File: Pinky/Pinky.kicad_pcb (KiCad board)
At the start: 2 copper layers, 142.2 x 120.5 mm, 79 parts, among them J1 MJ-4PP-9, J4 LED, P1 i2c-pin, P2 i2c-pin, SW1 RESET_SW, SW10 SW_PUSH, SW11 SW_PUSH, SW12 SW_PUSH, SW13 SW_PUSH, SW14 SW_PUSH, SW15 SW_PUSH, SW16 SW_PUSH, SW17 SW_PUSH, SW18 SW_PUSH, SW19 SW_PUSH, SW2 SW_PUSH, SW20 SW_PUSH, SW21 SW_PUSH, SW22 SW_PUSH, SW23 SW_PUSH, SW24 SW_PUSH, SW25 SW_PUSH, SW26 SW_PUSH, SW27 SW_PUSH, SW28 SW_PUSH, SW29 SW_PUSH, SW3 SW_PUSH, SW30 SW_PUSH, SW31 SW_PUSH, SW32 SW_PUSH, SW33 SW_PUSH, SW4 SW_PUSH, SW5 SW_PUSH, SW6 SW_PUSH, SW7 SW_PUSH, SW8 SW_PUSH, SW9 SW_PUSH, U1 ProMicro

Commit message: finished wiring
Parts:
- removed J4: LED, kbd:StripLED_rev
- JP1: value Jumper -> JP
- moved JP1 4.81 mm to (82.2, 133.8)
- moved D31 1.90 mm to (164.3, 104.2)
- moved D22 0.28 mm to (129.6, 119.7)
- moved D15 0.20 mm to (107.2, 90.2)
- moved D21 0.10 mm to (126.2, 96.5)
- turned R1 to 180 degrees
- turned R2 to 180 degrees
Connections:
- U1 pad 1: led -> Net-(U1-Pad1)
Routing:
- net GND: track 6.44 -> 179.2 mm, vias 0 -> 34
- net VCC: track 29.3 -> 151.1 mm, vias 0 -> 1
- net col6: track 184.9 -> 298.2 mm, vias 6 -> 8
- net Net-(J1-PadB): track 6.44 -> 115.2 mm, vias 0 -> 1
- net col5: track 185.0 -> 289.9 mm, vias 6 -> 7
- net row3: track 94.7 -> 182.5 mm, vias 0 -> 1
- net row0: track 159.4 -> 231.3 mm, vias 0 -> 1
- net row4: track 63.7 -> 125.2 mm, vias 0 -> 2
- net data: track 0.00 -> 53.4 mm, vias 0 -> 1
- net reset: track 0.00 -> 50.5 mm, vias 0 -> 1
- net sda: track 0.00 -> 47.1 mm, vias 0 -> 1
- net scl: track 0.00 -> 44.5 mm, vias 0 -> 1
- net Net-(D4-Pad2): track 61.8 -> 18.6 mm, vias 4 -> 1
- net col3: track 221.7 -> 255.6 mm, vias 6 -> 7
- net col4: track 236.8 -> 270.4 mm, vias 9 -> 7
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- added copper zone on B.Cu, net GND
- added copper zone on F.Cu, net GND
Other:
- net class Default: via_dia 0.8 -> 0.6
- board text added: "ver. 0.1.0. @tamanishi"

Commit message: add top plate layer
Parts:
- moved D26 0.05 mm to (145.2, 100.2)
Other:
- board text added: "rev. 0.1 @tamanishi"
- board text removed: "ver. 0.1.0. @tamanishi"
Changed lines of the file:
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@@
   (general
     (thickness 1.6)
-    (drawings 151)
+    (drawings 172)
     (tracks 1427)
     (zones 0)
@@
   (page A4)
   (layers
-    (0 F.Cu signal hide)
-    (31 B.Cu signal hide)
+    (0 F.Cu signal)
+    (31 B.Cu signal)
     (32 B.Adhes user hide)
     (33 F.Adhes user hide)
-    (34 B.Paste user hide)
+    (34 B.Paste user)
     (35 F.Paste user hide)
-    (36 B.SilkS user hide)
-    (37 F.SilkS user hide)
+    (36 B.SilkS user)
+    (37 F.SilkS user)
     (38 B.Mask user hide)
     (39 F.Mask user hide)
@@
     (41 Cmts.User user hide)
     (42 Eco1.User user hide)
-    (43 Eco2.User user)
+    (43 Eco2.User user hide)
     (44 Edge.Cuts user)
     (45 Margin user hide)
@@
     (pad_to_mask_clearance 0.051)
     (solder_mask_min_width 0.25)
-    (aux_axis_origin 0 0)
+    (aux_axis_origin 40.3 35.2)
     (visible_elements FFFFFF3F)
     (pcbplotparams
@@
   )
   (module kbd:D3_TH_SMD (layer F.Cu)
-    (at 145.2 100.2)
+    (at 145.25 100.2)
     (descr "Resitance 3 pas")
     (tags R)
@@
       (net 50 col6))
   )
-  (gr_text "ver. 0.1.0.\n@tamanishi" (at 83.2 121.2) (layer B.SilkS)
+  (dimension 142.2 (width 0.3) (layer Dwgs.User)
+    (gr_text "142.200 mm" (at 111.4 29.8) (layer Dwgs.User)
+      (effects (font (size 1.5 1.5) (thickness 0.3)))
+    )
+    (feature1 (pts (xy 182.5 35.2) (xy 182.5 31.313579)))
+    (feature2 (pts (xy 40.3 35.2) (xy 40.3 31.313579)))
+    (crossbar (pts (xy 40.3 31.9) (xy 182.5 31.9)))
+    (arrow1a (pts (xy 182.5 31.9) (xy 181.373496 32.486421)))
+    (arrow1b (pts (xy 182.5 31.9) (xy 181.373496 31.313579)))
+    (arrow2a (pts (xy 40.3 31.9) (xy 41.426504 32.486421)))
+    (arrow2b (pts (xy 40.3 31.9) (xy 41.426504 31.313579)))
+  )
+  (dimension 120.600165 (width 0.3) (layer Dwgs.User)
+    (gr_text "120.600 mm" (at 35 95.500082 270) (layer Dwgs.User)
+      (effects (font (size 1.5 1.5) (thickness 0.3)))
+    )
+    (feature1 (pts (xy 40.3 155.800165) (xy 36.513579 155.800165)))
+    (feature2 (pts (xy 40.3 35.2) (xy 36.513579 35.2)))
+    (crossbar (pts (xy 37.1 35.2) (xy 37.1 155.800165)))
+    (arrow1a (pts (xy 37.1 155.800165) (xy 36.513579 154.673661)))
+    (arrow1b (pts (xy 37.1 155.800165) (xy 37.686421 154.673661)))
+    (arrow2a (pts (xy 37.1 35.2) (xy 36.513579 36.326504)))
+    (arrow2b (pts (xy 37.1 35.2) (xy 37.686421 36.326504)))
+  )
+  (gr_arc (start 173.3 102.5) (end 173.3 103.2) (angle -90) (layer Dwgs.User) (width 0.15))
+  (gr_line (start 170.8 103.2) (end 173.3 103.2) (layer Dwgs.User) (width 0.15))
+  (gr_line (start 167.8 110.3) (end 170.8 103.2) (layer Dwgs.User) (width 0.15))
+  (gr_line (start 119.2 41.095) (end 133.2 41.095) (layer Dwgs.User) (width 0.15))
+  (gr_line (start 144.4 120.7) (end 117 116.5) (layer Dwgs.User) (width 0.15))
+  (gr_arc (start 171.500001 131.300001) (end 171.100002 132.1) (angle -90) (layer Dwgs.User) (width 0.15))
+  (gr_line (start 144.4 120.7) (end 171.1 132.1) (layer Dwgs.User) (width 0.15))
+  (gr_line (start 41 116.5) (end 117.1 116.5) (layer Dwgs.User) (width 0.15))
+  (gr_line (start 41.1 40.6) (end 98.1 35.2) (layer Dwgs.User) (width 0.15))
+  (gr_line (start 98.1 35.2) (end 116.2 35.2) (layer Dwgs.User) (width 0.15))
+  (gr_line (start 116.2 35.2) (end 173.3 46.4) (layer Dwgs.User) (width 0.15))
+  (gr_line (start 174 47.1) (end 174 102.5) (layer Dwgs.User) (width 0.15))
+  (gr_line (start 172.3 131.7) (end 179 115.9) (layer Dwgs.User) (width 0.15))
+  (gr_line (start 178.6 114.9) (end 167.8 110.3) (layer Dwgs.User) (width 0.15))
+  (gr_arc (start 41 115.8) (end 40.3 115.8) (angle -90) (layer Dwgs.User) (width 0.15))
+  (gr_arc (start 178.3 115.6) (end 179 115.9) (angle -90) (layer Dwgs.User) (width 0.15))
+  (gr_arc (start 173.2 47.2) (end 174 47.1) (angle -75.7) (layer Dwgs.User) (width 0.15))
+  (gr_arc (start 41.299999 41.599999) (end 41.1 40.6) (angle -69.2) (layer Dwgs.User) (width 0.15))
+  (gr_line (start 40.3 115.8) (end 40.3 41.4) (layer Dwgs.User) (width 0.15))
+  (gr_text "rev. 0.1\n@tamanishi" (at 83.2 121.2) (layer B.SilkS)
     (effects (font (size 1.5 1.5) (thickness 0.3)) (justify mirror))
   )
-  (gr_text "ver. 0.1.0.\n@tamanishi" (at 83.2 121.2) (layer F.SilkS)
+  (gr_text "rev. 0.1\n@tamanishi" (at 83.2 121.2) (layer F.SilkS)
     (effects (font (size 1.5 1.5) (thickness 0.3)))
   )

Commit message: tweaked wiring
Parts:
- moved Ref** 3.01 mm to (151.6, 119.5)
- turned JP1 to 90 degrees
- turned SW32 to 157 degrees
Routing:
- net col6: track 298.2 -> 284.3 mm
- net (no net): track 0.00 -> 6.29 mm
- net Net-(D31-Pad2): track 30.1 -> 25.0 mm, vias 2 -> 0
- net Net-(J1-PadB): track 115.2 -> 112.1 mm
- net GND: track 179.2 -> 178.1 mm, vias 34 -> 32

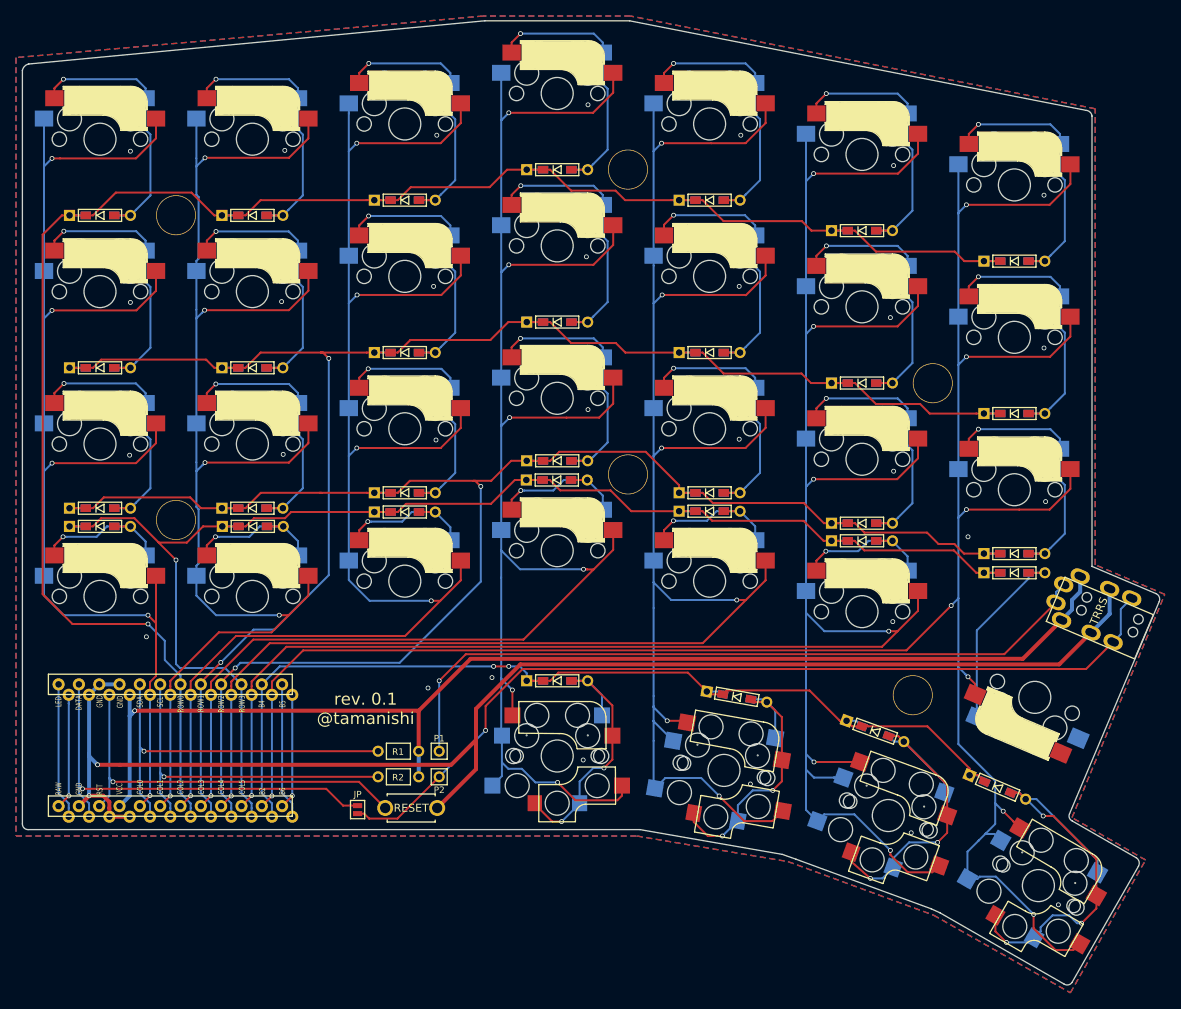
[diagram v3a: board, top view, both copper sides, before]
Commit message: change direction of some keyswitches and tweak wiring
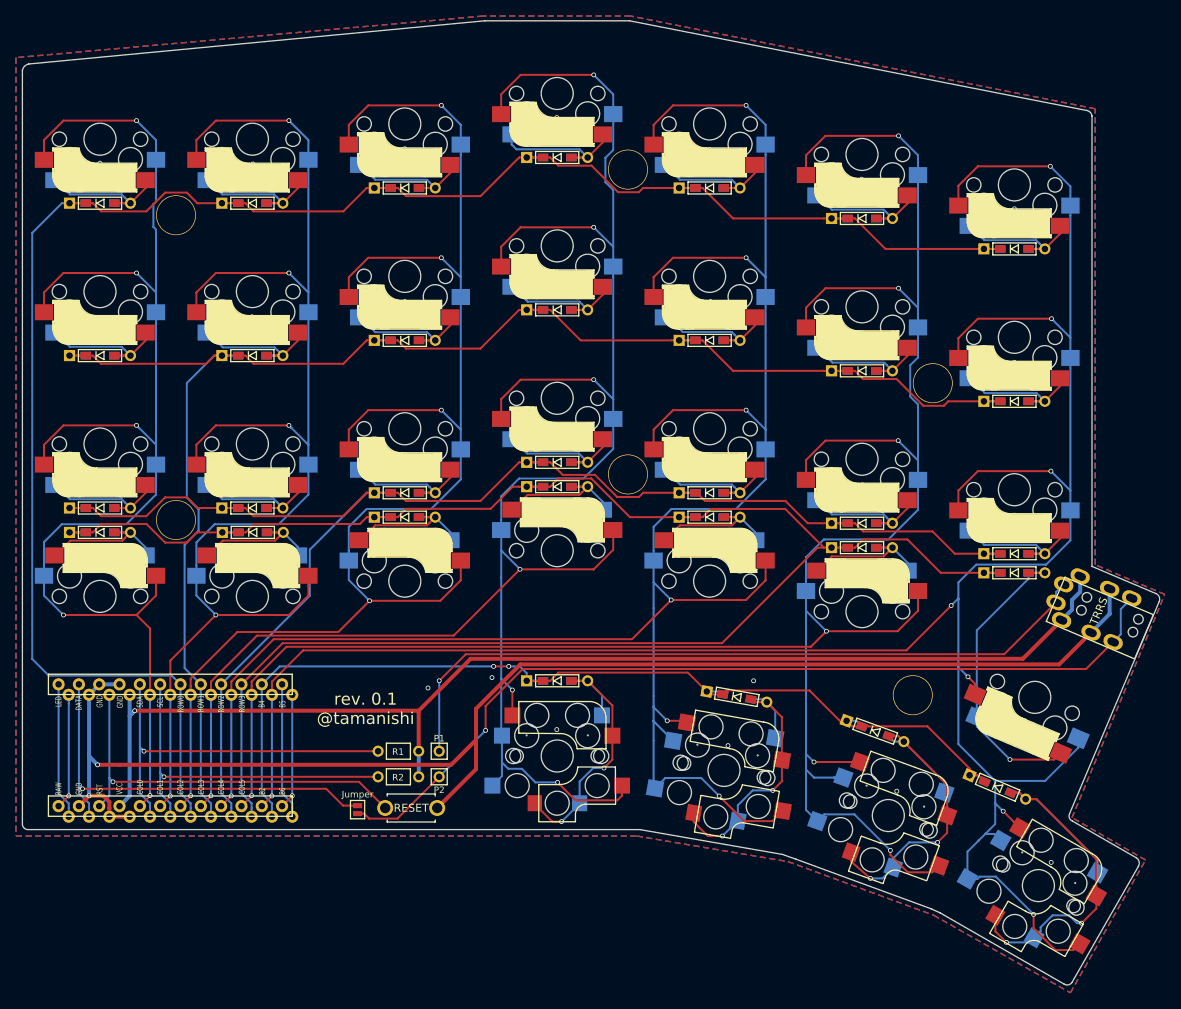
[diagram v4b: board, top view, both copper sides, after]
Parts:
- JP1: value JP -> Jumper
- moved D10 1.53 mm to (88.1, 75.1)
- moved D13 1.53 mm to (107.2, 52.3)
- moved D14 1.53 mm to (107.2, 71.3)
- moved D19 1.53 mm to (126.2, 75.1)
- moved D2 1.53 mm to (50.0, 77.0)
- moved D24 1.53 mm to (145.2, 79.0)
- moved D29 1.53 mm to (164.3, 82.8)
- moved D6 1.53 mm to (69.0, 77.0)
- moved D1 1.52 mm to (50.0, 58.0)
- moved D18 1.52 mm to (126.2, 56.1)
- moved D23 1.52 mm to (145.2, 59.9)
- moved D5 1.52 mm to (69.0, 58.0)
- moved D9 1.52 mm to (88.1, 56.1)
- moved D28 1.52 mm to (164.3, 63.7)
- moved D26 0.86 mm to (145.2, 101.1)
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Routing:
- net row3: track 182.5 -> 238.8 mm, vias 1 -> 0
- net col6: track 284.3 -> 307.4 mm
- net row2: track 208.8 -> 191.6 mm, vias 2 -> 0
- net Net-(D2-Pad2): track 35.0 -> 18.4 mm, vias 1 -> 0
- net Net-(D19-Pad2): track 35.0 -> 18.4 mm, vias 1 -> 0
- net Net-(D24-Pad2): track 34.9 -> 18.4 mm, vias 1 -> 0
- net Net-(D23-Pad2): track 34.9 -> 18.4 mm, vias 1 -> 0
- net Net-(D9-Pad2): track 34.9 -> 18.4 mm, vias 1 -> 0
- net Net-(D18-Pad2): track 34.9 -> 18.4 mm, vias 1 -> 0
- net Net-(D28-Pad2): track 34.9 -> 18.4 mm, vias 1 -> 0
- net Net-(D29-Pad2): track 34.9 -> 18.4 mm, vias 1 -> 0
- net Net-(D10-Pad2): track 34.9 -> 18.4 mm, vias 1 -> 0
- net Net-(D14-Pad2): track 34.9 -> 18.4 mm, vias 1 -> 0
- net Net-(D6-Pad2): track 34.9 -> 18.4 mm, vias 1 -> 0
- net Net-(D5-Pad2): track 34.8 -> 18.4 mm, vias 1 -> 0
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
